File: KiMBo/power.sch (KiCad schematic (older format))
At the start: 30 parts

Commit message: Annotate all components, now passing ERC, added ferrites to the rest of the connectors
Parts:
- removed SW?: POWER, symbol SW_DPST_Small
- removed TP? (x4): TP, symbol TP
- removed U?: 74LVC1G07, symbol 74LVC1G07
- added SW2: Power, symbol SW_DPST_Passive
- added TP1, TP2, TP3, TP4: Test_Point, symbol Test_Point
- added U3: 74LVC1G06, symbol 74LVC1G06
- gave numbers to parts that had none: 21
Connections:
- net BAT_TEMP: now also TP2.1
- net BAT_VOLT: now also TP3.1
- net GND: now also SW2.1, SW2.3, TP1.1, U3.5
- net PMTC_PGOOD: now also U3.2
- net PWR_BUT: now also U2.D20 (PMIC_IN_PB_IN), SW2.2, SW2.4; no longer U2.D19 (PMIC_IN_PWR_EN)
- net VDD_1V8: now also U3.3
- net VIN_BAT: now also TP4.1
- net ~SYS_RESET: now also U3.4
- net at U2.C6 (PMIC_POWER_EN): now also U2.D19 (PMIC_IN_PWR_EN); no longer U2.D20 (PMIC_IN_PB_IN)
- no-connect marks 58 -> 60
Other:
- moved on the sheet: C6, R13, SW1

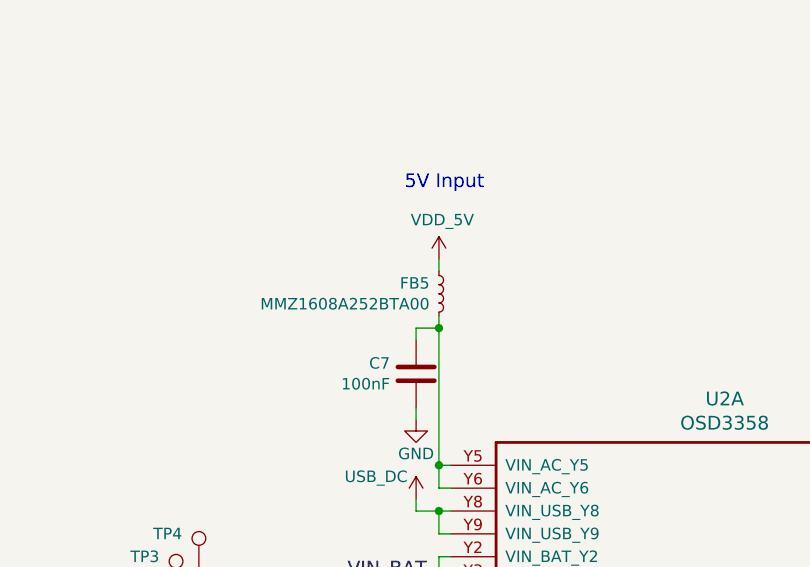
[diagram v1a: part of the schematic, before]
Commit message: Clean up various parts of the schematic, high level sheet has annoated modules
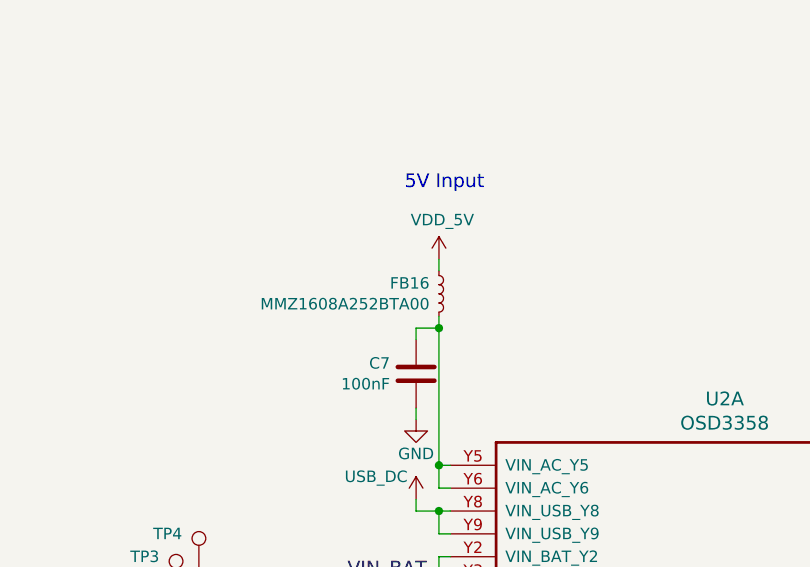
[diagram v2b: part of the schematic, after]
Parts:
- renumbered FB5 to FB16
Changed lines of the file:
@@
 TPS65217C\nOutput
 $Comp
-L INDUCTOR_Small FB5
+L INDUCTOR_Small FB16
 U 1 1 5AF7107F
 P 6900 4000
-F 0 "FB5" H 6859 3954 50  0000 R CNN
+F 0 "FB16" H 6859 3954 50  0000 R CNN
 F 1 "MMZ1608A252BTA00" H 6859 4045 50  0000 R CNN
 F 2 "" H 6900 4000 50  0000 C CNN
@@
 F 3 "" H 6800 4550 50  0000 C CNN
 	1    6800 4550
+	1    0    0    -1
+$EndComp
+Text HLabel 6750 6850 0    60   Input ~ 0
+I2C0_SCL
+Text HLabel 6750 6950 0    60   BiDi ~ 0
+I2C0_SDA
+NoConn ~ 12800 4600
+NoConn ~ 6250 6050
+$Comp
+L SW_DPST_Passive SW2
+U 1 1 5BB582A2
+P 5950 6050
+F 0 "SW2" H 5950 6250 50  0000 C CNN
+F 1 "Power" H 5950 5875 50  0000 C CNN
+F 2 "" H 5950 6050 50  0000 C CNN
+F 3 "" H 5950 6050 50  0000 C CNN
+	1    5950 6050
+	1    0    0    -1
+$EndComp
+$Comp
+L 74LVC1G06 U3
+U 1 1 5BB5D4E4
+P 5100 5950
+F 0 "U3" H 5350 5800 50  0000 R CNN
+F 1 "74LVC1G06" H 4900 5800 50  0000 R CNN
+F 2 "" H 5100 5950 50  0000 C CNN
+F 3 "" H 5100 5950 50  0000 C CNN
+	1    5100 5950
+	-1   0    0    1
+$EndComp
+$Comp
+L Test_Point TP4
+U 1 1 5BB5EE88
+P 5850 5200
+F 0 "TP4" H 5650 5350 50  0000 L CNN
+F 1 "Test_Point" H 5908 5229 50  0001 L CNN
+F 2 "" H 6050 5200 50  0000 C CNN
+F 3 "" H 6050 5200 50  0000 C CNN
+	1    5850 5200
+	1    0    0    -1
+$EndComp
+$Comp
+L Test_Point TP3
+U 1 1 5BB5EF8B
+P 5750 5300
+F 0 "TP3" H 5550 5450 50  0000 L CNN
+F 1 "Test_Point" H 5808 5329 50  0001 L CNN
+F 2 "" H 5950 5300 50  0000 C CNN
+F 3 "" H 5950 5300 50  0000 C CNN
+	1    5750 5300
+	1    0    0    -1
+$EndComp
+$Comp
+L Test_Point TP2
+U 1 1 5BB5F011
+P 5650 5400
+F 0 "TP2" H 5450 5550 50  0000 L CNN
+F 1 "Test_Point" H 5708 5429 50  0001 L CNN
+F 2 "" H 5850 5400 50  0000 C CNN
+F 3 "" H 5850 5400 50  0000 C CNN
+	1    5650 5400
+	1    0    0    -1
+$EndComp
+$Comp
+L Test_Point TP1
+U 1 1 5BB5F090
+P 5550 5500
+F 0 "TP1" H 5350 5650 50  0000 L CNN
+F 1 "Test_Point" H 5608 5529 50  0001 L CNN
+F 2 "" H 5750 5500 50  0000 C CNN
+F 3 "" H 5750 5500 50  0000 C CNN
+	1    5550 5500
 	1    0    0    -1
 $EndComp
@@
 Wire Wire Line
 	5550 5550 5550 5500
-Text HLabel 6750 6850 0    60   Input ~ 0
-I2C0_SCL
-Text HLabel 6750 6950 0    60   BiDi ~ 0
-I2C0_SDA
 Wire Wire Line
 	6800 4150 6900 4150
 Wire Wire Line
 	6800 4950 6950 4950
-NoConn ~ 12800 4600
-NoConn ~ 6250 6050
 Wire Wire Line
 	6950 5650 6900 5650
 Wire Wire Line
 	6900 5650 6900 5550
-$Comp
-L SW_DPST_Passive SW2
-U 1 1 5BB582A2
-P 5950 6050
-F 0 "SW2" H 5950 6250 50  0000 C CNN
-F 1 "Power" H 5950 5875 50  0000 C CNN
-F 2 "" H 5950 6050 50  0000 C CNN
-F 3 "" H 5950 6050 50  0000 C CNN
-	1    5950 6050
-	1    0    0    -1
-$EndComp
-$Comp
-L 74LVC1G06 U3
-U 1 1 5BB5D4E4
-P 5100 5950
-F 0 "U3" H 5350 5800 50  0000 R CNN
-F 1 "74LVC1G06" H 4900 5800 50  0000 R CNN
-F 2 "" H 5100 5950 50  0000 C CNN
-F 3 "" H 5100 5950 50  0000 C CNN
-	1    5100 5950
-	-1   0    0    1
-$EndComp
-$Comp
-L Test_Point TP4
-U 1 1 5BB5EE88
-P 5850 5200
-F 0 "TP4" H 5650 5350 50  0000 L CNN
-F 1 "Test_Point" H 5908 5229 50  0001 L CNN
-F 2 "" H 6050 5200 50  0000 C CNN
-F 3 "" H 6050 5200 50  0000 C CNN
-	1    5850 5200
-	1    0    0    -1
-$EndComp
-$Comp
-L Test_Point TP3
-U 1 1 5BB5EF8B
-P 5750 5300
-F 0 "TP3" H 5550 5450 50  0000 L CNN
-F 1 "Test_Point" H 5808 5329 50  0001 L CNN
-F 2 "" H 5950 5300 50  0000 C CNN
-F 3 "" H 5950 5300 50  0000 C CNN
-	1    5750 5300
-	1    0    0    -1
-$EndComp
-$Comp
-L Test_Point TP2
-U 1 1 5BB5F011
-P 5650 5400
-F 0 "TP2" H 5450 5550 50  0000 L CNN
-F 1 "Test_Point" H 5708 5429 50  0001 L CNN
-F 2 "" H 5850 5400 50  0000 C CNN
-F 3 "" H 5850 5400 50  0000 C CNN
-	1    5650 5400
-	1    0    0    -1
-$EndComp
-$Comp
-L Test_Point TP1
-U 1 1 5BB5F090
-P 5550 5500
-F 0 "TP1" H 5350 5650 50  0000 L CNN
-F 1 "Test_Point" H 5608 5529 50  0001 L CNN
-F 2 "" H 5750 5500 50  0000 C CNN
-F 3 "" H 5750 5500 50  0000 C CNN
-	1    5550 5500
-	1    0    0    -1
-$EndComp
 $EndSCHEMATC

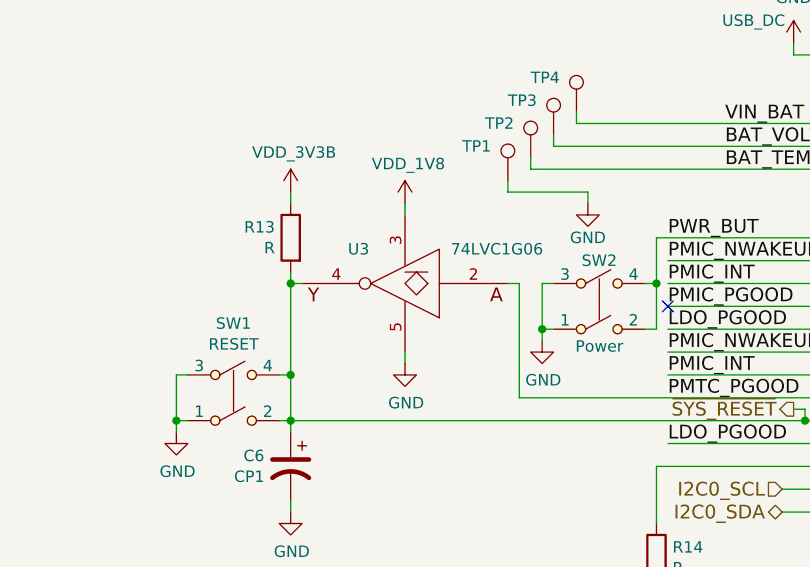
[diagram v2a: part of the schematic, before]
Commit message: Reorder the SS and EN lines from the shift registers such that the previously enabled/disabled motors stay enabled/disabled whilst writting to the shift register
Change 10k resistors to 4.7k, flip the open-drain inverter connected to B15 (PMTC_PGOOD)

Update the links in the README

Update the PDF schematic
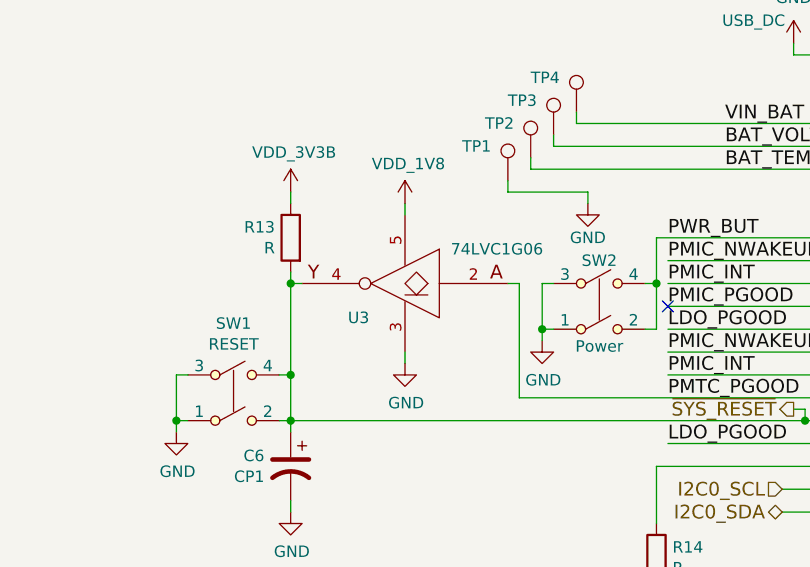
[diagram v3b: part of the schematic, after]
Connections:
- net GND: now also U3.3; no longer U3.5
- net VDD_1V8: now also U3.5; no longer U3.3
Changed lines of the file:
@@
 F 0 "SW1" H 4350 6775 50  0000 C CNN
 F 1 "RESET" H 4350 6684 50  0000 C CNN
-F 2 "" H 4350 6450 50  0000 C CNN
+F 2 "" H 4350 6450 50  0001 C CNN
 F 3 "" H 4350 6450 50  0000 C CNN
 	1    4350 6450
@@
 F 0 "C6" H 4715 6796 50  0000 L CNN
 F 1 "CP1" H 4715 6705 50  0000 L CNN
-F 2 "" H 4600 6750 50  0000 C CNN
+F 2 "" H 4600 6750 50  0001 C CNN
 F 3 "" H 4600 6750 50  0000 C CNN
 	1    4600 6750
@@
 F 0 "R13" H 4669 5796 50  0000 L CNN
 F 1 "R" H 4669 5705 50  0000 L CNN
-F 2 "" V 4530 5750 50  0000 C CNN
+F 2 "" V 4530 5750 50  0001 C CNN
 F 3 "" H 4600 5750 50  0000 C CNN
 	1    4600 5750
@@
 F 0 "D7" V 10396 6692 50  0000 R CNN
 F 1 "LED" V 10305 6692 50  0000 R CNN
-F 2 "" H 10350 6800 50  0000 C CNN
+F 2 "" H 10350 6800 50  0001 C CNN
 F 3 "" H 10350 6800 50  0000 C CNN
 	1    10350 6800
@@
 F 0 "R17" H 10420 7246 50  0000 L CNN
 F 1 "R" H 10420 7155 50  0000 L CNN
-F 2 "" V 10280 7200 50  0000 C CNN
+F 2 "" V 10280 7200 50  0001 C CNN
 F 3 "" H 10350 7200 50  0000 C CNN
 	1    10350 7200
@@
 F 0 "R14" H 6270 7196 50  0000 L CNN
 F 1 "R" H 6270 7105 50  0000 L CNN
-F 2 "" V 6130 7150 50  0000 C CNN
+F 2 "" V 6130 7150 50  0001 C CNN
 F 3 "" H 6200 7150 50  0000 C CNN
 	1    6200 7150
@@
 F 0 "R15" H 10069 2296 50  0000 L CNN
 F 1 "R" H 10069 2205 50  0000 L CNN
-F 2 "" V 9930 2250 50  0000 C CNN
+F 2 "" V 9930 2250 50  0001 C CNN
 F 3 "" H 10000 2250 50  0000 C CNN
 	1    10000 2250
@@
 F 0 "Q1" H 9941 2404 50  0000 L CNN
 F 1 "Q_PNP_BCE" H 9941 2495 50  0000 L CNN
-F 2 "" H 9950 2550 50  0000 C CNN
+F 2 "" H 9950 2550 50  0001 C CNN
 F 3 "" H 9750 2450 50  0000 C CNN
 	1    9750 2450
@@
 F 0 "R16" V 9993 2450 50  0000 C CNN
 F 1 "R" V 10084 2450 50  0000 C CNN
-F 2 "" V 10130 2450 50  0000 C CNN
+F 2 "" V 10130 2450 50  0001 C CNN
 F 3 "" H 10200 2450 50  0000 C CNN
 	1    10200 2450
@@
 F 0 "R18" H 10470 2296 50  0000 L CNN
 F 1 "R" H 10470 2205 50  0000 L CNN
-F 2 "" V 10330 2250 50  0000 C CNN
+F 2 "" V 10330 2250 50  0001 C CNN
 F 3 "" H 10400 2250 50  0000 C CNN
 	1    10400 2250
@@
 F 0 "R19" H 10470 2796 50  0000 L CNN
 F 1 "R" H 10470 2705 50  0000 L CNN
-F 2 "" V 10330 2750 50  0000 C CNN
+F 2 "" V 10330 2750 50  0001 C CNN
 F 3 "" H 10400 2750 50  0000 C CNN
 	1    10400 2750
@@
 F 0 "R20" H 11519 2296 50  0000 L CNN
 F 1 "R" H 11519 2205 50  0000 L CNN
-F 2 "" V 11380 2250 50  0000 C CNN
+F 2 "" V 11380 2250 50  0001 C CNN
 F 3 "" H 11450 2250 50  0000 C CNN
 	1    11450 2250
@@
 F 0 "Q2" H 11391 2404 50  0000 L CNN
 F 1 "Q_PNP_BCE" H 11391 2495 50  0000 L CNN
-F 2 "" H 11400 2550 50  0000 C CNN
+F 2 "" H 11400 2550 50  0001 C CNN
 F 3 "" H 11200 2450 50  0000 C CNN
 	1    11200 2450
@@
 F 0 "R21" V 11443 2450 50  0000 C CNN
 F 1 "R" V 11534 2450 50  0000 C CNN
-F 2 "" V 11580 2450 50  0000 C CNN
+F 2 "" V 11580 2450 50  0001 C CNN
 F 3 "" H 11650 2450 50  0000 C CNN
 	1    11650 2450
@@
 F 0 "R22" H 11920 2296 50  0000 L CNN
 F 1 "R" H 11920 2205 50  0000 L CNN
-F 2 "" V 11780 2250 50  0000 C CNN
+F 2 "" V 11780 2250 50  0001 C CNN
 F 3 "" H 11850 2250 50  0000 C CNN
 	1    11850 2250
@@
 F 0 "R23" H 11920 2796 50  0000 L CNN
 F 1 "R" H 11920 2705 50  0000 L CNN
-F 2 "" V 11780 2750 50  0000 C CNN
+F 2 "" V 11780 2750 50  0001 C CNN
 F 3 "" H 11850 2750 50  0000 C CNN
 	1    11850 2750
@@
 F 0 "D6" V 9954 2621 50  0000 R CNN
 F 1 "TVH431" V 10045 2621 50  0000 R CNN
-F 2 "" H 10000 2700 50  0000 C CNN
+F 2 "" H 10000 2700 50  0001 C CNN
 F 3 "" H 10000 2700 50  0000 C CNN
 	1    10000 2700
@@
 F 0 "D8" V 11404 2621 50  0000 R CNN
 F 1 "TVH431" V 11495 2621 50  0000 R CNN
-F 2 "" H 11450 2700 50  0000 C CNN
+F 2 "" H 11450 2700 50  0001 C CNN
 F 3 "" H 11450 2700 50  0000 C CNN
 	1    11450 2700
@@
 F 0 "FB16" H 6859 3954 50  0000 R CNN
 F 1 "MMZ1608A252BTA00" H 6859 4045 50  0000 R CNN
-F 2 "" H 6900 4000 50  0000 C CNN
+F 2 "" H 6900 4000 50  0001 C CNN
 F 3 "" H 6900 4000 50  0000 C CNN
 	1    6900 4000
@@
 F 0 "C7" H 6914 4396 50  0000 L CNN
 F 1 "100nF" H 6914 4305 50  0000 L CNN
-F 2 "" H 6838 4200 50  0000 C CNN
+F 2 "" H 6838 4200 50  0001 C CNN
 F 3 "" H 6800 4350 50  0000 C CNN
 	1    6800 4350
@@
 F 0 "SW2" H 5950 6250 50  0000 C CNN
 F 1 "Power" H 5950 5875 50  0000 C CNN
-F 2 "" H 5950 6050 50  0000 C CNN
+F 2 "" H 5950 6050 50  0001 C CNN
 F 3 "" H 5950 6050 50  0000 C CNN
 	1    5950 6050
@@
 P 5100 5950
 F 0 "U3" H 5350 5800 50  0000 R CNN
-F 1 "74LVC1G06" H 4900 5800 50  0000 R CNN
-F 2 "" H 5100 5950 50  0000 C CNN
+F 1 "74LVC1G06" H 4900 6100 50  0000 R CNN
+F 2 "" H 5100 5950 50  0001 C CNN
 F 3 "" H 5100 5950 50  0000 C CNN
 	1    5100 5950
-	-1   0    0    1
+	-1   0    0    -1
 $EndComp
 $Comp
@@
 F 0 "TP4" H 5650 5350 50  0000 L CNN
 F 1 "Test_Point" H 5908 5229 50  0001 L CNN
-F 2 "" H 6050 5200 50  0000 C CNN
+F 2 "" H 6050 5200 50  0001 C CNN
 F 3 "" H 6050 5200 50  0000 C CNN
 	1    5850 5200
@@
 F 0 "TP3" H 5550 5450 50  0000 L CNN
 F 1 "Test_Point" H 5808 5329 50  0001 L CNN
-F 2 "" H 5950 5300 50  0000 C CNN
+F 2 "" H 5950 5300 50  0001 C CNN
 F 3 "" H 5950 5300 50  0000 C CNN
 	1    5750 5300
@@
 F 0 "TP2" H 5450 5550 50  0000 L CNN
 F 1 "Test_Point" H 5708 5429 50  0001 L CNN
-F 2 "" H 5850 5400 50  0000 C CNN
+F 2 "" H 5850 5400 50  0001 C CNN
 F 3 "" H 5850 5400 50  0000 C CNN
 	1    5650 5400
@@
 F 0 "TP1" H 5350 5650 50  0000 L CNN
 F 1 "Test_Point" H 5608 5529 50  0001 L CNN
-F 2 "" H 5750 5500 50  0000 C CNN
+F 2 "" H 5750 5500 50  0001 C CNN
 F 3 "" H 5750 5500 50  0000 C CNN
 	1    5550 5500

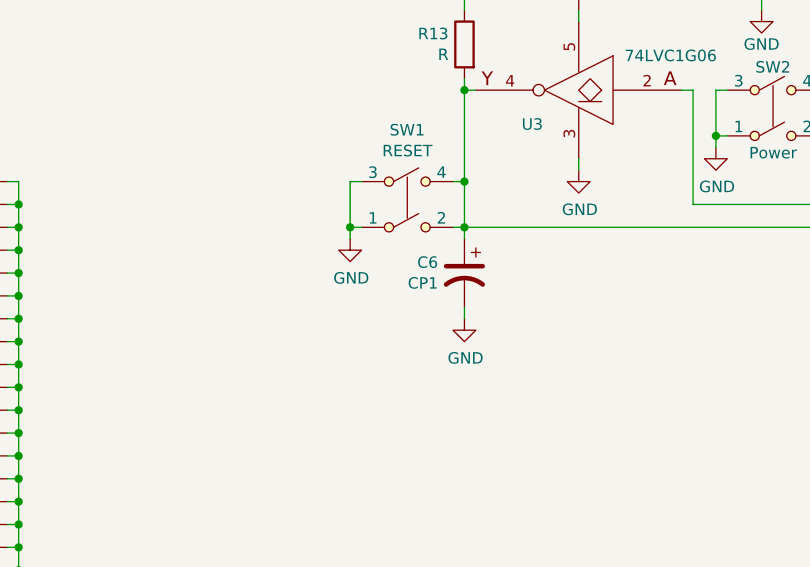
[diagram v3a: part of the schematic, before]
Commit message: Begin entry of component values
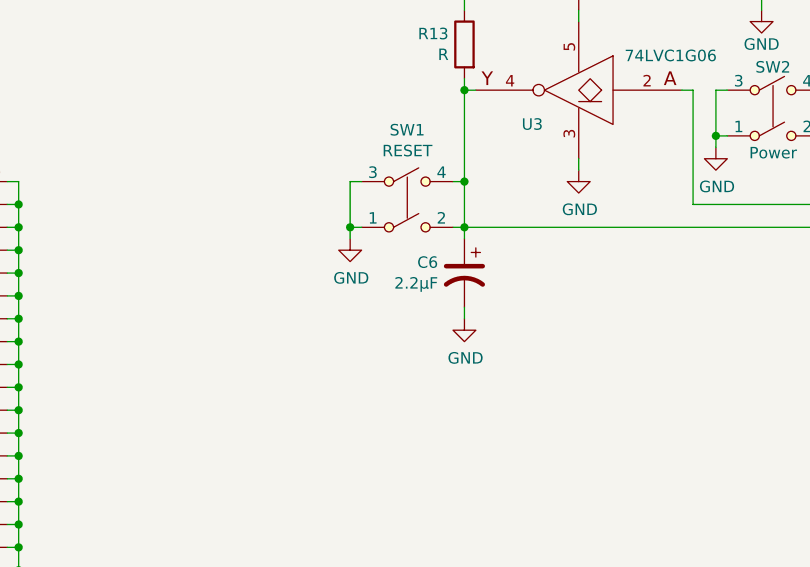
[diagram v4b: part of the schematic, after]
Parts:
- C6: value CP1 -> 2.2μF
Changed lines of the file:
@@
 P 4600 6750
 F 0 "C6" H 4715 6796 50  0000 L CNN
-F 1 "CP1" H 4715 6705 50  0000 L CNN
+F 1 "2.2μF" H 4715 6705 50  0000 L CNN
 F 2 "" H 4600 6750 50  0001 C CNN
 F 3 "" H 4600 6750 50  0000 C CNN
